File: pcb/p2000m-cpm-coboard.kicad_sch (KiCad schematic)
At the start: 24 parts, among them J1 CPU BOARD, J2 EXPANSION BOARD, J3 T/~{M}, J4 POWER, J5 TERMINAL, U1 CY62256-70PC, U2 SST39SF010, U3 DIL16, U4 74LS74, U5 74LS138, U6 74LS283, U7 82S123, U8 74LS02

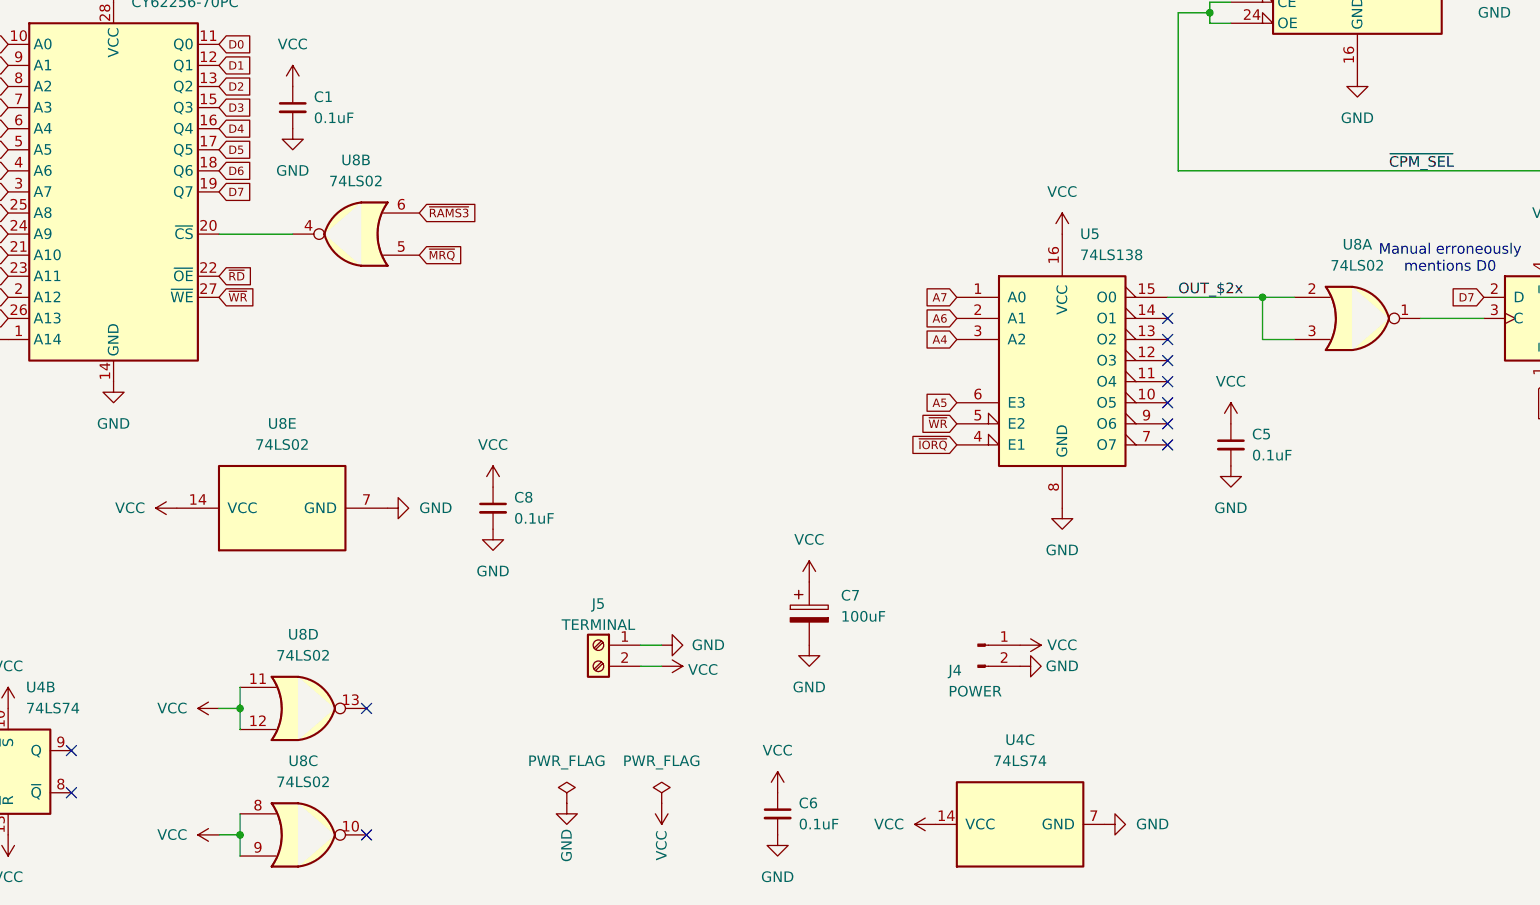
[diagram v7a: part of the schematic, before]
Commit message: Fixing bug in wiring
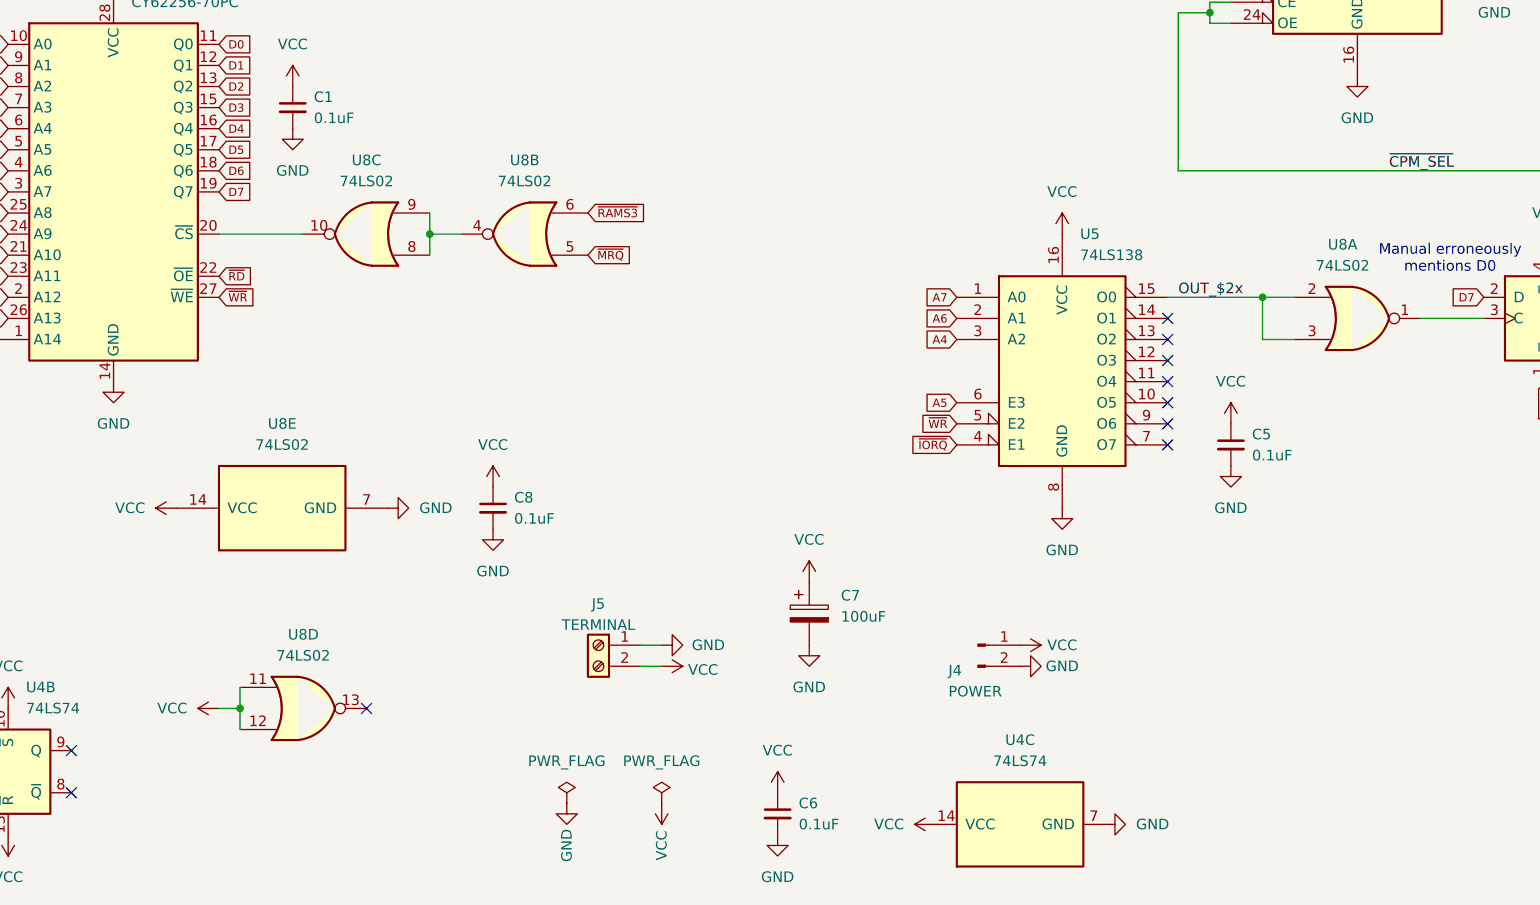
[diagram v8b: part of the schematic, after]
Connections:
- net VCC: no longer U8.8, U8.9
- net at U8.4: now also U8.8, U8.9; no longer U1.20 (~{CS})
- net at U8.10: now also U1.20 (~{CS})
- no-connect marks 17 -> 16
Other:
- moved on the sheet: U8B, U8C
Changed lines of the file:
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@@
 	)
 	(junction
-		(at 59.69 187.96)
-		(diameter 0)
-		(color 0 0 0 0)
-	)
-	(junction
 		(at 175.26 49.53)
 		(diameter 0)
@@
 	)
 	(junction
+		(at 82.55 115.57)
+		(diameter 0)
+		(color 0 0 0 0)
+	)
+	(junction
 		(at 214.63 31.75)
 		(diameter 0)
@@
 	)
 	(no_connect
-		(at 74.93 187.96)
-	)
-	(no_connect
 		(at 137.16 60.96)
 	)
@@
 	(wire
 		(pts
-			(xy 57.15 115.57) (xy 66.04 115.57)
+			(xy 57.15 115.57) (xy 67.31 115.57)
 		)
 		(stroke
@@
 	(wire
 		(pts
-			(xy 57.15 187.96) (xy 59.69 187.96)
-		)
-		(stroke
-			(width 0)
-			(type default)
-		)
-	)
-	(wire
-		(pts
 			(xy 57.15 172.72) (xy 59.69 172.72)
 		)
@@
 	(wire
 		(pts
-			(xy 59.69 187.96) (xy 59.69 185.42)
-		)
-		(stroke
-			(width 0)
-			(type default)
-		)
-	)
-	(wire
-		(pts
 			(xy 59.69 172.72) (xy 59.69 175.26)
 		)
@@
 	(wire
 		(pts
+			(xy 82.55 115.57) (xy 86.36 115.57)
+		)
+		(stroke
+			(width 0)
+			(type default)
+		)
+	)
+	(wire
+		(pts
+			(xy 82.55 115.57) (xy 82.55 118.11)
+		)
+		(stroke
+			(width 0)
+			(type default)
+		)
+	)
+	(wire
+		(pts
 			(xy 227.33 44.45) (xy 238.76 44.45)
 		)
@@
 	(wire
 		(pts
+			(xy 82.55 113.03) (xy 82.55 115.57)
+		)
+		(stroke
+			(width 0)
+			(type default)
+		)
+	)
+	(wire
+		(pts
 			(xy 175.26 72.39) (xy 175.26 69.85)
 		)
@@
 	(wire
 		(pts
-			(xy 59.69 187.96) (xy 59.69 190.5)
-		)
-		(stroke
-			(width 0)
-			(type default)
-		)
-	)
-	(wire
-		(pts
 			(xy 219.71 29.21) (xy 219.71 36.83)
 		)
@@
 	(global_label "~{MRQ}"
 		(shape input)
-		(at 81.28 118.11 0)
+		(at 101.6 118.11 0)
 		(fields_autoplaced yes)
 		(effects
@@
 		)
 		(property "Intersheetrefs" "${INTERSHEET_REFS}"
-			(at 86.8208 118.11 0)
+			(at 107.1408 118.11 0)
 			(hide yes)
 			(show_name no)
@@
 	(global_label "~{RAMS3}"
 		(shape input)
-		(at 81.28 113.03 0)
+		(at 101.6 113.03 0)
 		(fields_autoplaced yes)
 		(effects
@@
 		)
 		(property "Intersheetrefs" "${INTERSHEET_REFS}"
-			(at 88.6511 113.03 0)
+			(at 108.9711 113.03 0)
 			(hide yes)
 			(show_name no)
@@
 		(in_pos_files yes)
 		(dnp no)
-		(fields_autoplaced yes)
 		(property "Reference" "U8"
-			(at 194.31 116.84 0)
+			(at 192.532 116.84 0)
 			(show_name no)
 			(do_not_autoplace no)
@@
 		)
 		(property "Value" "74LS02"
-			(at 194.31 119.38 0)
+			(at 192.532 119.38 0)
 			(show_name no)
 			(do_not_autoplace no)
@@
 	(symbol
 		(lib_id "74xx:74LS02")
-		(at 73.66 115.57 180)
+		(at 93.98 115.57 180)
 		(unit 2)
 		(body_style 1)
@@
 		(fields_autoplaced yes)
 		(property "Reference" "U8"
-			(at 73.66 106.68 0)
+			(at 93.98 106.68 0)
 			(show_name no)
 			(do_not_autoplace no)
@@
 		)
 		(property "Value" "74LS02"
-			(at 73.66 109.22 0)
+			(at 93.98 109.22 0)
 			(show_name no)
 			(do_not_autoplace no)
@@
 		)
 		(property "Footprint" "Package_DIP:DIP-14_W7.62mm_Socket"
-			(at 73.66 115.57 0)
+			(at 93.98 115.57 0)
 			(hide yes)
 			(show_name no)
@@
 		)
 		(property "Datasheet" "http://www.ti.com/lit/gpn/sn74ls02"
-			(at 73.66 115.57 0)
+			(at 93.98 115.57 0)
 			(hide yes)
 			(show_name no)
@@
 		)
 		(property "Description" "quad 2-input NOR gate"
-			(at 73.66 115.57 0)
+			(at 93.98 115.57 0)
 			(hide yes)
 			(show_name no)
@@
 	)
 	(symbol
-		(lib_id "power:VCC")
-		(at 57.15 187.96 90)
-		(unit 1)
-		(body_style 1)
-		(exclude_from_sim no)
-		(in_bom yes)
-		(on_board yes)
-		(in_pos_files yes)
-		(dnp no)
-		(fields_autoplaced yes)
-		(property "Reference" "#PWR057"
-			(at 60.96 187.96 0)
-			(hide yes)
-			(show_name no)
-			(do_not_autoplace no)
-			(effects
-				(font
-					(size 1.27 1.27)
-				)
-			)
-		)
-		(property "Value" "VCC"
-			(at 53.34 187.9599 90)
-			(show_name no)
-			(do_not_autoplace no)
-			(effects
-				(font
-					(size 1.27 1.27)
-				)
-				(justify left)
-			)
-		)
-		(property "Footprint" ""
-			(at 57.15 187.96 0)
-			(hide yes)
-			(show_name no)
-			(do_not_autoplace no)
-			(effects
-				(font
-					(size 1.27 1.27)
-				)
-			)
-		)
-		(property "Datasheet" ""
-			(at 57.15 187.96 0)
-			(hide yes)
-			(show_name no)
-			(do_not_autoplace no)
-			(effects
-				(font
-					(size 1.27 1.27)
-				)
-			)
-		)
-		(property "Description" "Power symbol creates a global label with name \"VCC\""
-			(at 57.15 187.96 0)
-			(hide yes)
-			(show_name no)
-			(do_not_autoplace no)
-			(effects
-				(font
-					(size 1.27 1.27)
-				)
-			)
-		)
-		(pin "1"
-		)
-		(instances
-			(project "p2000m-cpm-coboard"
-				(path "/6fd0ac56-88c2-4ff6-8529-422939feb5ef"
-					(reference "#PWR057")
-					(unit 1)
-				)
-			)
-		)
-	)
-	(symbol
 		(lib_id "power:GND")
 		(at 110.49 165.1 90)
@@
 	(symbol
 		(lib_id "74xx:74LS02")
-		(at 67.31 187.96 0)
+		(at 74.93 115.57 180)
 		(unit 3)
 		(body_style 1)
@@
 		(fields_autoplaced yes)
 		(property "Reference" "U8"
-			(at 67.31 179.07 0)
+			(at 74.93 106.68 0)
 			(show_name no)
 			(do_not_autoplace no)
@@
 		)
 		(property "Value" "74LS02"
-			(at 67.31 181.61 0)
+			(at 74.93 109.22 0)
 			(show_name no)
 			(do_not_autoplace no)
@@
 		)
 		(property "Footprint" "Package_DIP:DIP-14_W7.62mm_Socket"
-			(at 67.31 187.96 0)
+			(at 74.93 115.57 0)
 			(hide yes)
 			(show_name no)
@@
 		)
 		(property "Datasheet" "http://www.ti.com/lit/gpn/sn74ls02"
-			(at 67.31 187.96 0)
+			(at 74.93 115.57 0)
 			(hide yes)
 			(show_name no)
@@
 		)
 		(property "Description" "quad 2-input NOR gate"
-			(at 67.31 187.96 0)
+			(at 74.93 115.57 0)
 			(hide yes)
 			(show_name no)
